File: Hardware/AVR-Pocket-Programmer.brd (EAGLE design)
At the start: 47 x 30.5 mm, 38 parts, among them Q1 12 MHz, U1 ATTINY2313-20S, U2 74ACT125D, X2 USBSMD

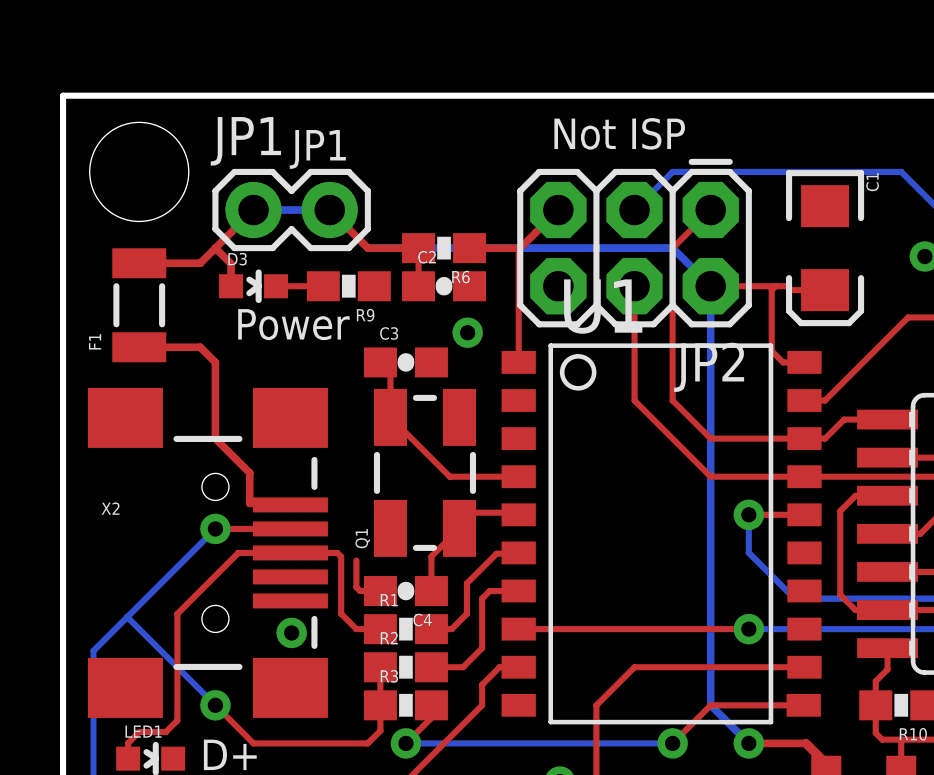
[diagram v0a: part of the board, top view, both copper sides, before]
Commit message: QC Revision - second round
In addition to the three previous changes:

1.) Updated PTC footprint
2.) General schematic cleanup
3.) OSHW and Creative Commons info
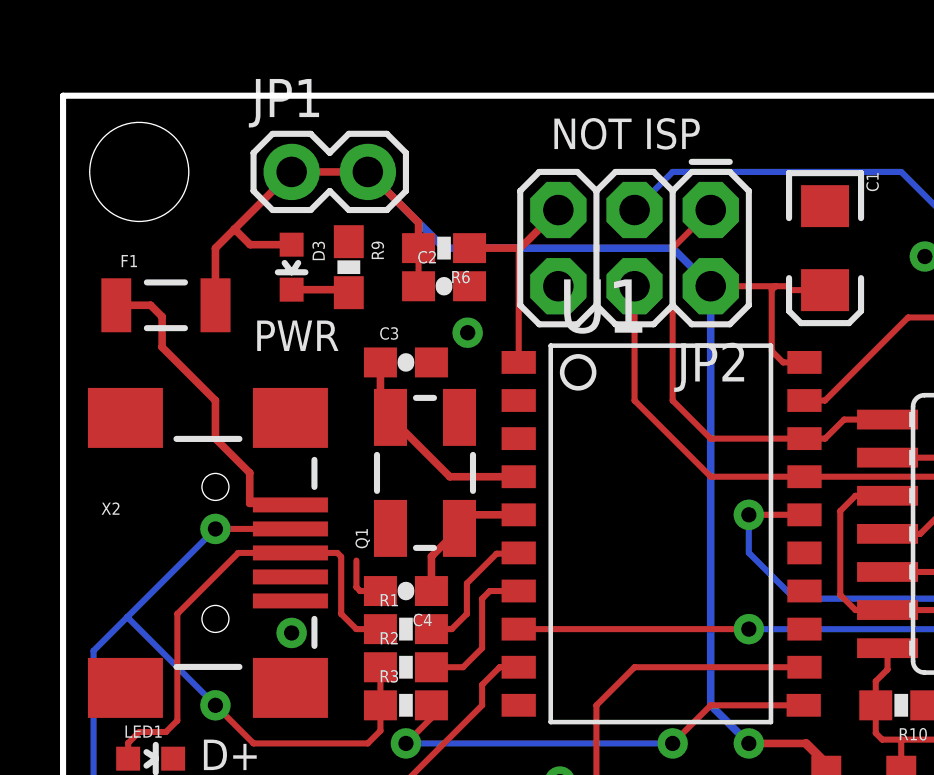
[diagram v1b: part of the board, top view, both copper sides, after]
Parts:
- removed U$10: (no value), SparkFun-Aesthetics:OSHW-LOGO-M
- removed U$9: CREATIVE_COMMONS, SparkFun:CREATIVE_COMMONS
- added FRAME1: FRAME-LETTER, SparkFun-Aesthetics:CREATIVE_COMMONS
- added LOGO1: OSHW-LOGOM, SparkFun-Aesthetics:OSHW-LOGO-M
- F1: device SparkFun:PTC-1206 -> SparkFun-PowerIC:PTC-1206-WIDE
- moved JP1 1.80 mm to (7.62, 27.9)
- moved D3 1.42 mm to (7.62, 24.8), turned to 180 degrees
- moved F1 0.89 mm to (3.43, 23.5), turned to 0 degrees
- moved R9 0.64 mm to (9.53, 24.8), turned to 270 degrees
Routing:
- net N$4: track 9.59 -> 10.8 mm
- net VCC: track 53.3 -> 53.9 mm
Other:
- board text added: "NOT ISP"
- board text added: "PWR"
- board text added: "Revision: Kade Jensen"
- board text added: "SMD Design: N. Seidle"
- board text removed: "JP1"
- board text removed: "Not ISP"
